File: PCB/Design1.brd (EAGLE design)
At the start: 70 x 42 mm, 23 parts, among them J1 FTDI_DEVICE, U1 ATMEGA2560AU

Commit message: Update new Board
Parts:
- added CHARGE: (no value), SparkFun-Connectors:2X3
- added D2: (no value), SparkFun-DiscreteSemi:SMA-DIODE_ALT
- added R4: 470KΩ, SparkFun-Resistors:1206
- added R5: 100KΩ, SparkFun-Resistors:1206
- 5V: value 7805T -> 7805
- moved C9 31.0 mm to (-12.0, -24.0)
- moved C10 30.7 mm to (-13.0, -28.0)
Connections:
- net SERIAL0 renamed TX1
- net SERIAL1 renamed RX1
- net SERIAL2 renamed TX2
- net SERIAL3 renamed RX2
- new net RAW: D2.A, POWER.2
- new net VSENSE: R4.2, R5.1
- net GND: now also CHARGE.2, CHARGE.6, R5.2
- net VIN: now also D2.C, R4.1; no longer POWER.2
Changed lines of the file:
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@@
 <element name="POWER" library="SparkFun-Connectors" package="1X02_LOCK" value="" x="66" y="38" rot="R270"/>
 <element name="SERIAL" library="SparkFun-Connectors" package="2X4" value="" x="64" y="16"/>
-<element name="5V" library="linear" package="TO220H" value="7805T" x="-11" y="9"/>
+<element name="5V" library="linear" package="TO220H" value="7805" x="-11" y="9"/>
 <element name="AMS1117" library="SparkFun-PowerIC" package="SOT223" value="3.3V" x="-23" y="-6">
 <attribute name="PROD_ID" value="VREG-08170" x="-23" y="-6" size="1.778" layer="27" display="off"/>
@@
 <attribute name="PROD_ID" value="SWCH-08247" x="0" y="-8" size="1.778" layer="27" display="off"/>
 </element>
-<element name="C9" library="SparkFun-Capacitors" package="1206" value="10uF" x="-23" y="-53"/>
-<element name="C10" library="SparkFun-Capacitors" package="1206" value="0.1uF" x="-23" y="-57"/>
+<element name="C9" library="SparkFun-Capacitors" package="1206" value="10uF" x="-12" y="-24"/>
+<element name="C10" library="SparkFun-Capacitors" package="1206" value="0.1uF" x="-13" y="-28"/>
+<element name="CHARGE" library="SparkFun-Connectors" package="2X3" value="" x="6" y="-26">
+<attribute name="PROD_ID" value="CONN-11566" x="6" y="-26" size="1.778" layer="27" display="off"/>
+</element>
+<element name="D2" library="SparkFun-DiscreteSemi" package="SMA-DIODE_ALT" value="" x="-7" y="-17"/>
+<element name="R4" library="SparkFun-Resistors" package="1206" value="470KΩ" x="-6" y="-33"/>
+<element name="R5" library="SparkFun-Resistors" package="1206" value="100KΩ" x="0" y="-33"/>
 </elements>
 <signals>
@@
 <contactref element="C10" pad="2"/>
 <contactref element="AMS1117" pad="1"/>
+<contactref element="CHARGE" pad="2"/>
+<contactref element="CHARGE" pad="6"/>
+<contactref element="R5" pad="2"/>
 <wire x1="65.27" y1="17.27" x2="66" y2="38.1778" width="0" layer="19" extent="1-1"/>
 <wire x1="65.27" y1="14.73" x2="65.27" y2="17.27" width="0" layer="19" extent="1-1"/>
@@
 <wire x1="-21.6" y1="-25" x2="-21.6" y2="-22" width="0" layer="19" extent="1-1"/>
 <wire x1="-24.4" y1="-31" x2="-21.6" y2="-25" width="0" layer="19" extent="1-1"/>
-<wire x1="-21.6" y1="-53" x2="-24.4" y2="-31" width="0" layer="19" extent="1-1"/>
-<wire x1="-21.6" y1="-57" x2="-21.6" y2="-53" width="0" layer="19" extent="1-1"/>
+<wire x1="-11.6" y1="-28" x2="-21.6" y2="-25" width="0" layer="19" extent="1-1"/>
+<wire x1="-10.6" y1="-24" x2="-11.6" y2="-28" width="0" layer="19" extent="1-1"/>
+<wire x1="1.4" y1="-33" x2="-11.6" y2="-28" width="0" layer="19" extent="1-1"/>
+<wire x1="6" y1="-23.46" x2="1.4" y2="-33" width="0" layer="19" extent="1-1"/>
+<wire x1="11.08" y1="-23.46" x2="6" y2="-23.46" width="0" layer="19" extent="1-1"/>
 </signal>
 <signal name="N$1">
@@
 <contactref element="J1" pad="P$3"/>
 <wire x1="3" y1="30.73" x2="25.16" y2="30.93" width="0" layer="19" extent="1-1"/>
-</signal>
-<signal name="VIN">
-<contactref element="POWER" pad="2"/>
-<contactref element="5V" pad="1"/>
-<contactref element="C1" pad="1"/>
-<contactref element="C2" pad="1"/>
-<wire x1="-13.54" y1="-1.16" x2="66" y2="35.2822" width="0" layer="19" extent="1-1"/>
-<wire x1="-24.4" y1="-16" x2="-13.54" y2="-1.16" width="0" layer="19" extent="1-1"/>
-<wire x1="-24.4" y1="-22" x2="-24.4" y2="-16" width="0" layer="19" extent="1-1"/>
 </signal>
 <signal name="5V">
@@
 <contactref element="AMS1117" pad="4"/>
 <contactref element="AMS1117" pad="2"/>
-<wire x1="-23" y1="-2.901" x2="67.81" y2="17.27" width="0" layer="19" extent="1-1"/>
-<wire x1="-23" y1="-9.0988" x2="-23" y2="-2.901" width="0" layer="19" extent="1-1"/>
-<wire x1="-24.4" y1="-53" x2="-23" y2="-9.0988" width="0" layer="19" extent="1-1"/>
-<wire x1="-24.4" y1="-57" x2="-24.4" y2="-53" width="0" layer="19" extent="1-1"/>
-</signal>
-<signal name="SERIAL0">
+<wire x1="-13.4" y1="-24" x2="67.81" y2="17.27" width="0" layer="19" extent="1-1"/>
+<wire x1="-14.4" y1="-28" x2="-13.4" y2="-24" width="0" layer="19" extent="1-1"/>
+<wire x1="-23" y1="-9.0988" x2="-13.4" y2="-24" width="0" layer="19" extent="1-1"/>
+<wire x1="-23" y1="-2.901" x2="-23" y2="-9.0988" width="0" layer="19" extent="1-1"/>
+</signal>
+<signal name="TX1">
 <contactref element="U1" pad="46"/>
 <contactref element="SERIAL" pad="2"/>
 <wire x1="37.16" y1="17.43" x2="60.19" y2="17.27" width="0" layer="19" extent="1-1"/>
 </signal>
-<signal name="SERIAL1">
+<signal name="RX1">
 <contactref element="U1" pad="45"/>
 <contactref element="SERIAL" pad="4"/>
 <wire x1="36.66" y1="17.43" x2="62.73" y2="17.27" width="0" layer="19" extent="1-1"/>
 </signal>
-<signal name="SERIAL2">
+<signal name="TX2">
 <contactref element="U1" pad="13"/>
 <contactref element="SERIAL" pad="1"/>
 <wire x1="25.16" y1="25.43" x2="60.19" y2="14.73" width="0" layer="19" extent="1-1"/>
 </signal>
-<signal name="SERIAL3">
+<signal name="RX2">
 <contactref element="U1" pad="12"/>
 <contactref element="SERIAL" pad="3"/>
 <wire x1="25.16" y1="25.93" x2="62.73" y2="14.73" width="0" layer="19" extent="1-1"/>
 </signal>
+<signal name="VIN">
+<contactref element="5V" pad="1"/>
+<contactref element="C1" pad="1"/>
+<contactref element="C2" pad="1"/>
+<contactref element="D2" pad="C"/>
+<contactref element="R4" pad="1"/>
+<wire x1="-24.4" y1="-16" x2="-24.4" y2="-22" width="0" layer="19" extent="1-1"/>
+<wire x1="-13.54" y1="-1.16" x2="-24.4" y2="-16" width="0" layer="19" extent="1-1"/>
+<wire x1="-5" y1="-17" x2="-13.54" y2="-1.16" width="0" layer="19" extent="1-1"/>
+<wire x1="-7.4" y1="-33" x2="-5" y2="-17" width="0" layer="19" extent="1-1"/>
+</signal>
+<signal name="RAW">
+<contactref element="POWER" pad="2"/>
+<contactref element="D2" pad="A"/>
+<wire x1="-9" y1="-17" x2="66" y2="35.2822" width="0" layer="19" extent="1-1"/>
+</signal>
+<signal name="VSENSE">
+<contactref element="R4" pad="2"/>
+<contactref element="R5" pad="1"/>
+<wire x1="-1.4" y1="-33" x2="-4.6" y2="-33" width="0" layer="19" extent="1-1"/>
+</signal>
 </signals>

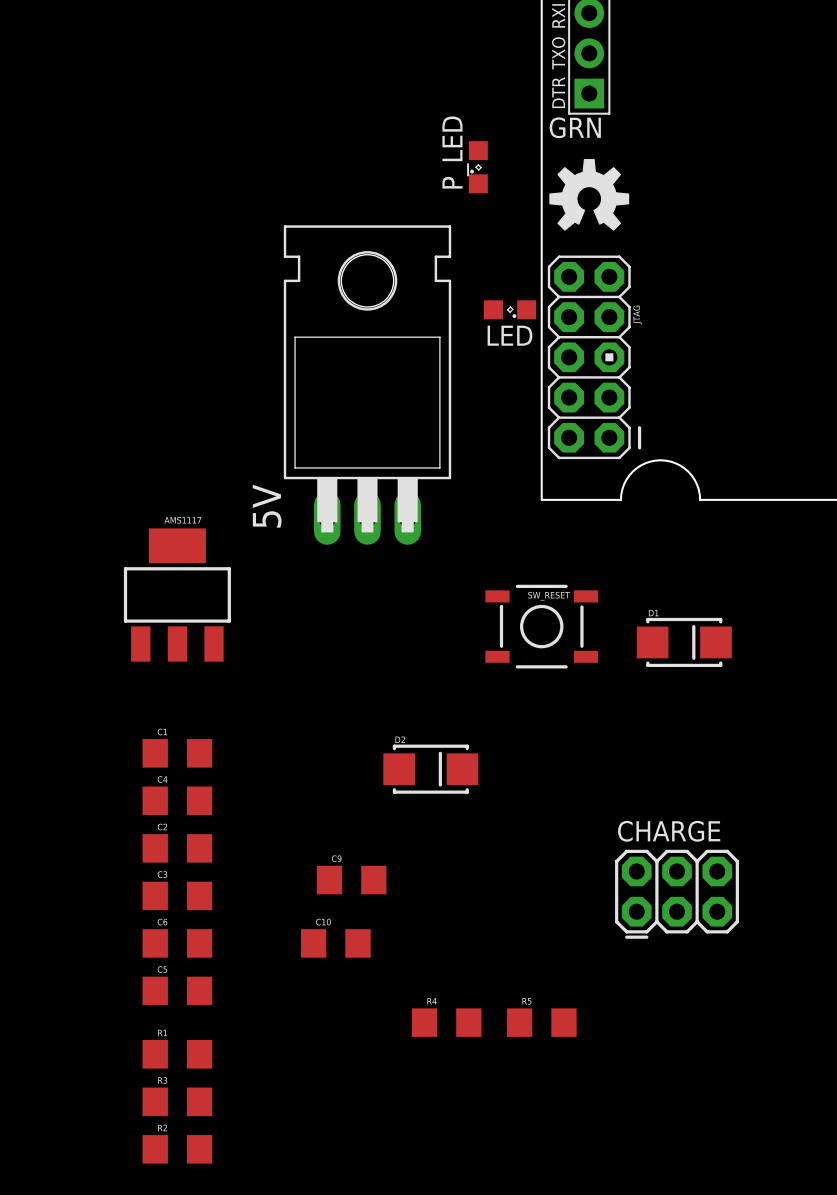
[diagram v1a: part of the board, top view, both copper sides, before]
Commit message: Add ICSP & Organize LEDs
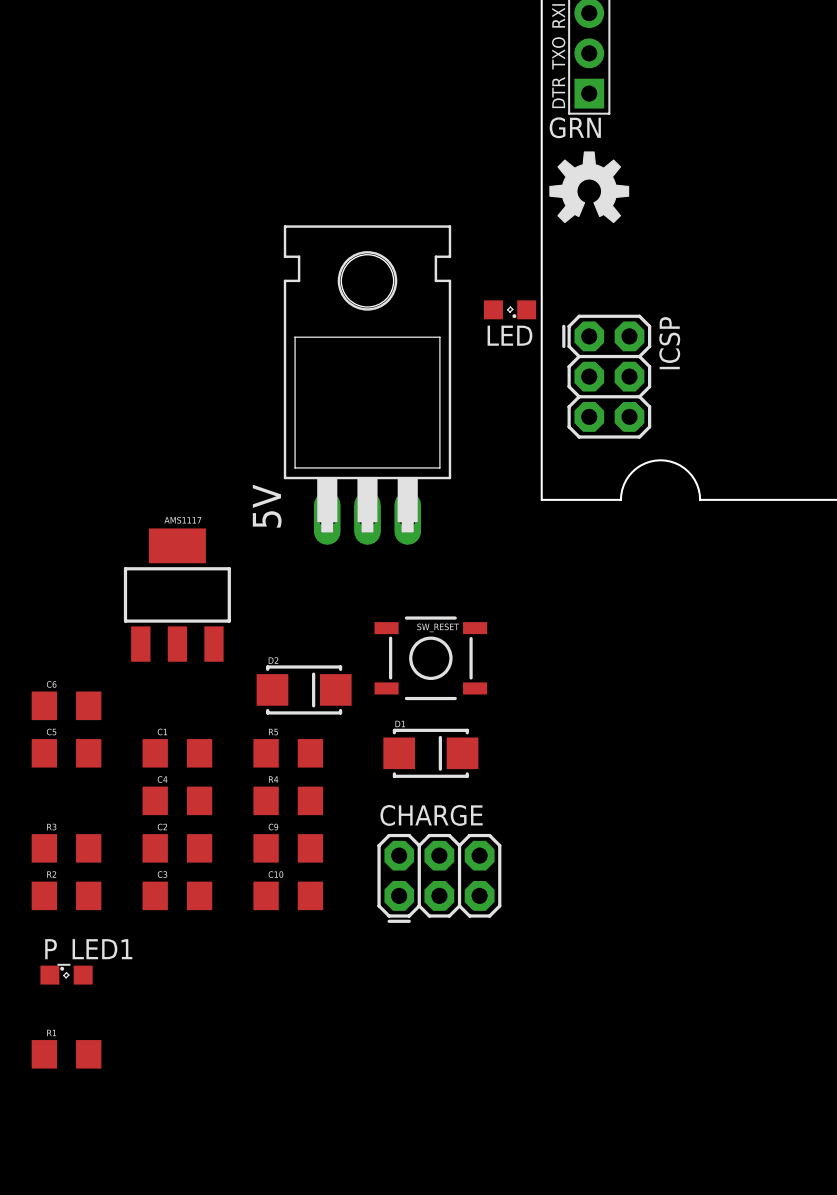
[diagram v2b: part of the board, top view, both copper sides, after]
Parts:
- removed JTAG: (no value), SparkFun-Connectors:AVR_ICSP
- removed P_LED: red, led:SML0805
- added ICSP: (no value), SparkFun-Connectors:2X3
- added P_LED1: red, led:SML0805
- moved R5 23.3 mm to (-16.0, -16.0)
- moved D1 17.5 mm to (-7.00, -16.0)
- moved R2 17.5 mm to (-30.0, -25.0)
- moved R3 17.5 mm to (-30.0, -22.0)
- moved R4 17.2 mm to (-16.0, -19.0)
- moved C5 16.6 mm to (-30.0, -16.0)
- moved C6 16.6 mm to (-30.0, -13.0)
- moved CHARGE 15.0 mm to (-9.00, -25.0)
- moved D2 9.43 mm to (-15.0, -12.0)
- moved SW_RESET 7.28 mm to (-7.00, -10.0)
- moved R1 7.00 mm to (-30.0, -35.0)
- moved C9 4.47 mm to (-16.0, -22.0)
- moved C10 4.24 mm to (-16.0, -25.0)
- moved LOGO1 0.48 mm to (3.00, 19.5)
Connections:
- removed net N$1: P_LED.A, R1.1
- new net CHARGE1: CHARGE.1
- new net CHARGE2: CHARGE.3
- new net CHARGE3: CHARGE.5
- new net MISO: ICSP.1, U1.22
- new net MOSI: ICSP.4, U1.21
- new net N$2: P_LED1.A, R1.1
- new net SCK: ICSP.3, U1.20
- net 5V: now also ICSP.2
- net DTR: now also ICSP.5
- net GND: now also CHARGE.4, ICSP.6, P_LED1.C; no longer P_LED.C

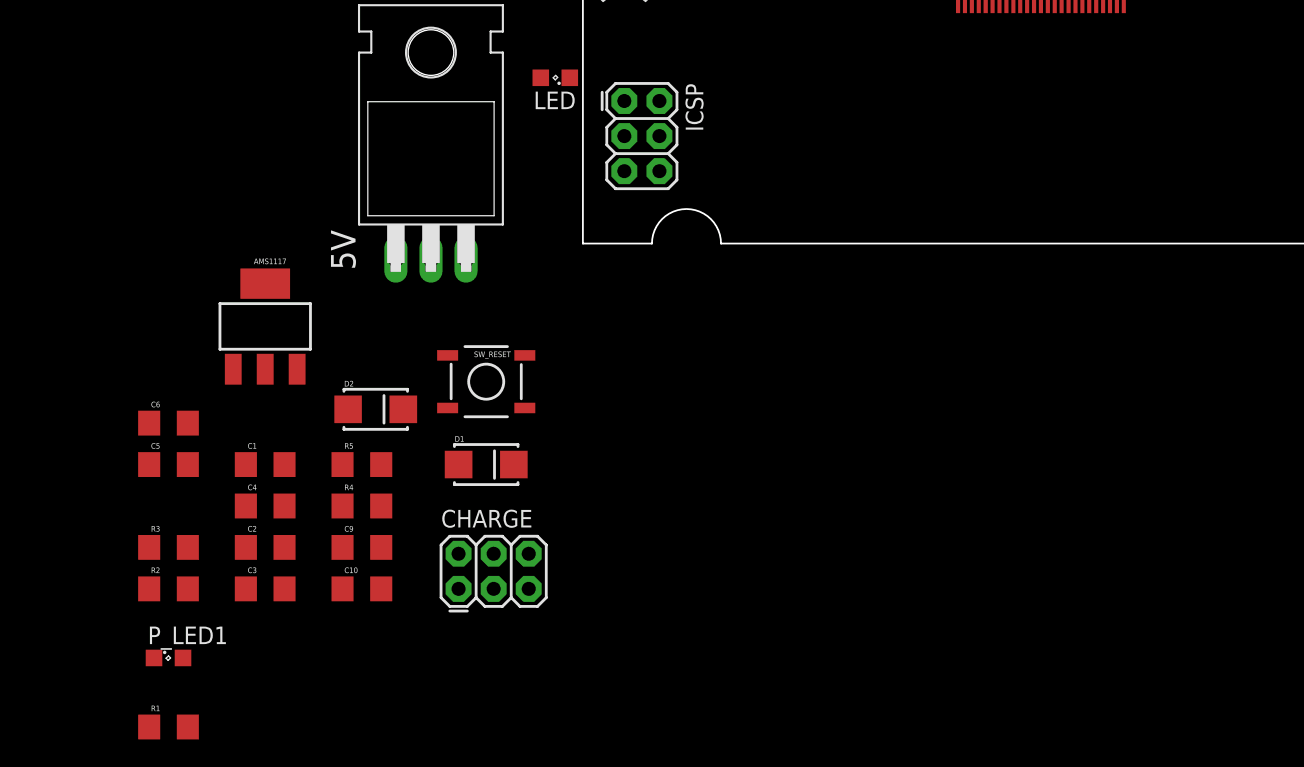
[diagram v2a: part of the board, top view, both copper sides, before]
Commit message: Ad LEDS, begin work on MOSFETs
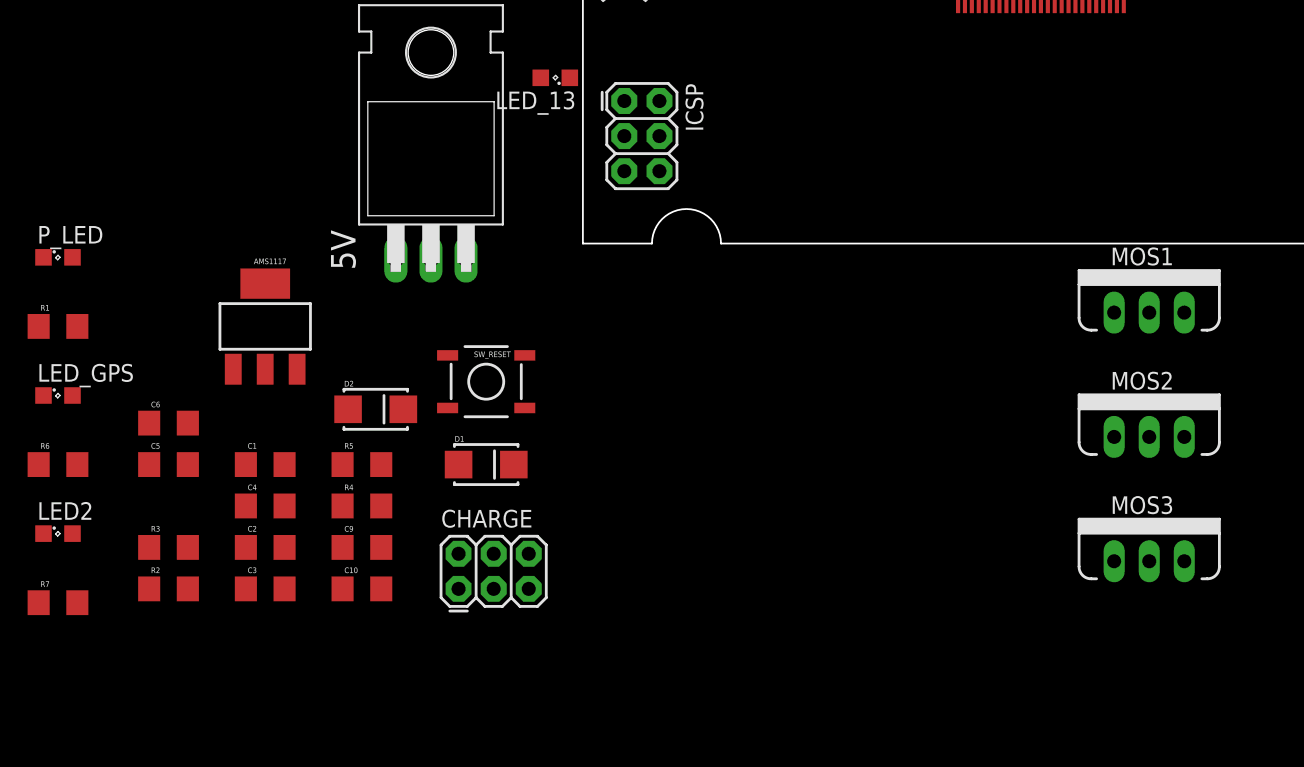
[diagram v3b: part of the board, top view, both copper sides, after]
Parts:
- removed P_LED1: red, led:SML0805
- added LED2: green, led:SML0805
- added LED_GPS: yellow, led:SML0805
- added MOS1, MOS2, MOS3: (no value), SparkFun-DiscreteSemi:TO220V
- added P_LED: red, led:SML0805
- added R6: 100Ω, SparkFun-Resistors:1206
- added R7: 150Ω, SparkFun-Resistors:1206
- LED_13: value yellow -> blue
- R3: value 100Ω -> 150Ω
- moved R1 30.1 mm to (-38.0, -6.00)
- renumbered LED to LED_13
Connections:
- net PIN13 renamed LED_13
- new net LED_: R7.2
- new net LED_GPS: R6.2
- new net N$1: LED_GPS.A, R6.1
- new net N$4: LED2.A, R7.1
- net GND: now also LED2.C, LED_GPS.C, MOS1.3, MOS2.3, MOS3.3, P_LED.C; no longer P_LED1.C
- net N$2: now also P_LED.A; no longer P_LED1.A
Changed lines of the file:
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@@
 <text x="57.12" y="13.68" size="1.778" layer="21">1
 2</text>
+<dimension x1="70" y1="42" x2="70" y2="0" x3="75" y3="21" textsize="1.778" layer="51" visible="yes"/>
+<dimension x1="0" y1="42" x2="70" y2="42" x3="35" y3="45" textsize="1.778" layer="51" visible="yes"/>
 </plain>
 <attributes>
@@
 <element name="D1" library="SparkFun-DiscreteSemi" package="SMA-DIODE_ALT" value="" x="-7" y="-16"/>
 <element name="LOGO1" library="SparkFun-Aesthetics" package="OSHW-LOGO-M" value="OSHW-LOGOM" x="3" y="19.48"/>
-<element name="LED" library="led" package="SML0805" value="yellow" x="-2" y="12" rot="R180"/>
+<element name="LED_13" library="led" package="SML0805" value="blue" x="-2" y="12" rot="R180"/>
 <element name="POWER" library="SparkFun-Connectors" package="1X02_LOCK" value="" x="66" y="38" rot="R270"/>
 <element name="SERIAL" library="SparkFun-Connectors" package="2X4" value="" x="64" y="16"/>
@@
 <element name="C6" library="SparkFun-Capacitors" package="1206" value="0.1uF" x="-30" y="-13"/>
 <element name="C5" library="SparkFun-Capacitors" package="1206" value="0.22uF" x="-30" y="-16"/>
-<element name="R3" library="SparkFun-Resistors" package="1206" value="100Ω" x="-30" y="-22"/>
+<element name="R3" library="SparkFun-Resistors" package="1206" value="150Ω" x="-30" y="-22"/>
 <element name="R2" library="SparkFun-Resistors" package="1206" value="10KΩ" x="-30" y="-25"/>
 <element name="SW_RESET" library="SparkFun-Electromechanical" package="TACTILE-SWITCH-SMD" value="" x="-7" y="-10">
@@
 <element name="R5" library="SparkFun-Resistors" package="1206" value="100KΩ" x="-16" y="-16"/>
 <element name="ICSP" library="SparkFun-Connectors" package="2X3" value="" x="3" y="10.32" rot="R270"/>
-<element name="P_LED1" library="led" package="SML0805" value="red" x="-30" y="-30"/>
-<element name="R1" library="SparkFun-Resistors" package="1206" value="100Ω" x="-30" y="-35"/>
+<element name="P_LED" library="led" package="SML0805" value="red" x="-38" y="-1"/>
+<element name="R1" library="SparkFun-Resistors" package="1206" value="100Ω" x="-38" y="-6"/>
+<element name="LED_GPS" library="led" package="SML0805" value="yellow" x="-38" y="-11"/>
+<element name="R6" library="SparkFun-Resistors" package="1206" value="100Ω" x="-38" y="-16"/>
+<element name="LED2" library="led" package="SML0805" value="green" x="-38" y="-21"/>
+<element name="R7" library="SparkFun-Resistors" package="1206" value="150Ω" x="-38" y="-26"/>
+<element name="MOS1" library="SparkFun-DiscreteSemi" package="TO220V" value="" x="41" y="-5">
+<attribute name="PROD_ID" value="TRANS-10060" x="41" y="-5" size="1.778" layer="27" display="off"/>
+</element>
+<element name="MOS2" library="SparkFun-DiscreteSemi" package="TO220V" value="" x="41" y="-14">
+<attribute name="PROD_ID" value="TRANS-10060" x="41" y="-14" size="1.778" layer="27" display="off"/>
+</element>
+<element name="MOS3" library="SparkFun-DiscreteSemi" package="TO220V" value="" x="41" y="-23">
+<attribute name="PROD_ID" value="TRANS-10060" x="41" y="-23" size="1.778" layer="27" display="off"/>
+</element>
 </elements>
 <signals>
@@
 <contactref element="J1" pad="P$6"/>
 <contactref element="J1" pad="P$5"/>
-<contactref element="LED" pad="C"/>
+<contactref element="LED_13" pad="C"/>
 <contactref element="POWER" pad="1"/>
 <contactref element="U1" pad="32"/>
@@
 <contactref element="CHARGE" pad="4"/>
 <contactref element="ICSP" pad="6"/>
-<contactref element="P_LED1" pad="C"/>
+<contactref element="P_LED" pad="C"/>
+<contactref element="LED2" pad="C"/>
+<contactref element="LED_GPS" pad="C"/>
+<contactref element="MOS1" pad="3"/>
+<contactref element="MOS3" pad="3"/>
+<contactref element="MOS2" pad="3"/>
 <wire x1="65.27" y1="17.27" x2="66" y2="38.1778" width="0" layer="19" extent="1-1"/>
 <wire x1="65.27" y1="14.73" x2="65.27" y2="17.27" width="0" layer="19" extent="1-1"/>
@@
 <wire x1="-25.3114" y1="-9.0988" x2="-21.6" y2="-16" width="0" layer="19" extent="1-1"/>
 <wire x1="-31.4" y1="-16" x2="-25.3114" y2="-9.0988" width="0" layer="19" extent="1-1"/>
-<wire x1="-31.05" y1="-30" x2="-21.6" y2="-25" width="0" layer="19" extent="1-1"/>
+<wire x1="-39.05" y1="-21" x2="-31.4" y2="-16" width="0" layer="19" extent="1-1"/>
+<wire x1="-39.05" y1="-11" x2="-31.4" y2="-16" width="0" layer="19" extent="1-1"/>
+<wire x1="-39.05" y1="-1" x2="-39.05" y2="-11" width="0" layer="19" extent="1-1"/>
+<wire x1="43.54" y1="-5" x2="30.16" y2="17.43" width="0" layer="19" extent="1-1"/>
+<wire x1="43.54" y1="-14" x2="43.54" y2="-5" width="0" layer="19" extent="1-1"/>
+<wire x1="43.54" y1="-23" x2="43.54" y2="-14" width="0" layer="19" extent="1-1"/>
 </signal>
 <signal name="RESET">
@@
 <wire x1="3" y1="25.65" x2="3" y2="5.24" width="0" layer="19" extent="1-1"/>
 </signal>
-<signal name="PIN13">
+<signal name="LED_13">
 <contactref element="R3" pad="2"/>
 <contactref element="U1" pad="26"/>
@@
 </signal>
 <signal name="N$3">
-<contactref element="LED" pad="A"/>
+<contactref element="LED_13" pad="A"/>
 <contactref element="R3" pad="1"/>
 <wire x1="-3.05" y1="12" x2="-31.4" y2="-22" width="0" layer="19" extent="1-1"/>
@@
 <wire x1="-24.4" y1="-19" x2="-20.6886" y2="-9.0988" width="0" layer="19" extent="1-1"/>
 <wire x1="-24.4" y1="-25" x2="-24.4" y2="-19" width="0" layer="19" extent="1-1"/>
-<wire x1="-28.6" y1="-35" x2="-24.4" y2="-25" width="0" layer="19" extent="1-1"/>
+<wire x1="-36.6" y1="-6" x2="-20.6886" y2="-9.0988" width="0" layer="19" extent="1-1"/>
 </signal>
 <signal name="3.3V">
@@
 </signal>
 <signal name="N$2">
-<contactref element="P_LED1" pad="A"/>
+<contactref element="P_LED" pad="A"/>
 <contactref element="R1" pad="1"/>
-<wire x1="-28.95" y1="-30" x2="-31.4" y2="-35" width="0" layer="19" extent="1-1"/>
+<wire x1="-36.95" y1="-1" x2="-39.4" y2="-6" width="0" layer="19" extent="1-1"/>
+</signal>
+<signal name="N$1">
+<contactref element="LED_GPS" pad="A"/>
+<contactref element="R6" pad="1"/>
+<wire x1="-36.95" y1="-11" x2="-39.4" y2="-16" width="0" layer="19" extent="1-1"/>
+</signal>
+<signal name="N$4">
+<contactref element="LED2" pad="A"/>
+<contactref element="R7" pad="1"/>
+<wire x1="-36.95" y1="-21" x2="-39.4" y2="-26" width="0" layer="19" extent="1-1"/>
+</signal>
+<signal name="LED_GPS">
+<contactref element="R6" pad="2"/>
+</signal>
+<signal name="LED_">
+<contactref element="R7" pad="2"/>
 </signal>
 </signals>
